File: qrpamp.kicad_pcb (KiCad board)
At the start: 2 copper layers, 106 parts, among them K1 BAND3_IN, K2 BAND2_IN, K3 BAND1_IN, K4 BAND3_OUT, K5 BAND2_OUT, K6 BAND1_OUT, K7 ANT_RLY, P1 PWR, P2 PWR_SW, P3 SWD, P4 ANT, P5 RADIO, P6 PTT_IN, P7 Thumb-Joystick, Q1 MMBT6427, Q2 MMBF170, Q3 IRF510, Q4 IRF510, SW1 SW_PUSH, T1 8:8, T2 8:8, T3 2:3, T4 12:1, T5 1:12, U1 LM7805, U2 LM3940, U3 LCD-2x16, U4 STM32F401xB/C-LQFP

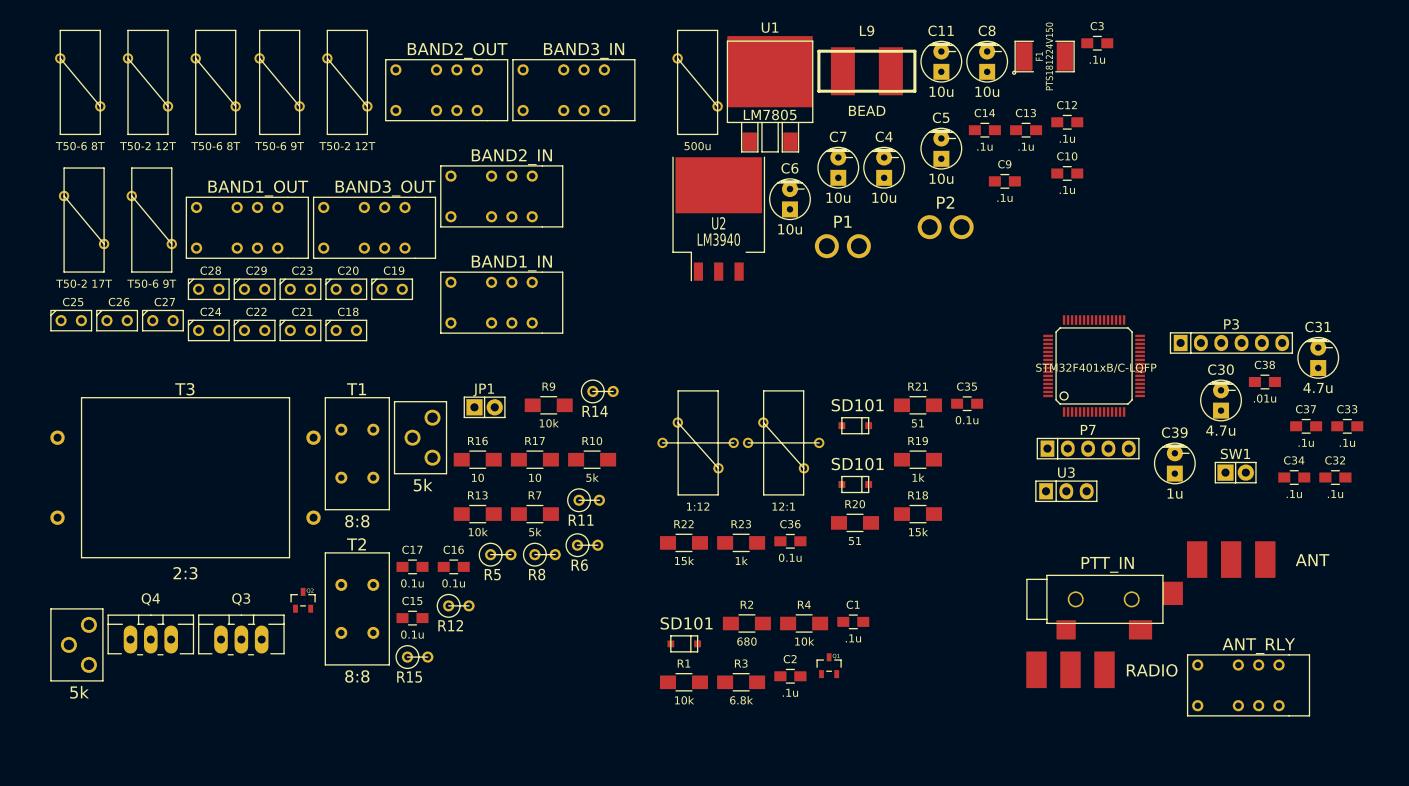
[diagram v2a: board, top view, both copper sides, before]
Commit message: All layed out
Several net errors fixed, and some mcu pins reassigned for better layout.
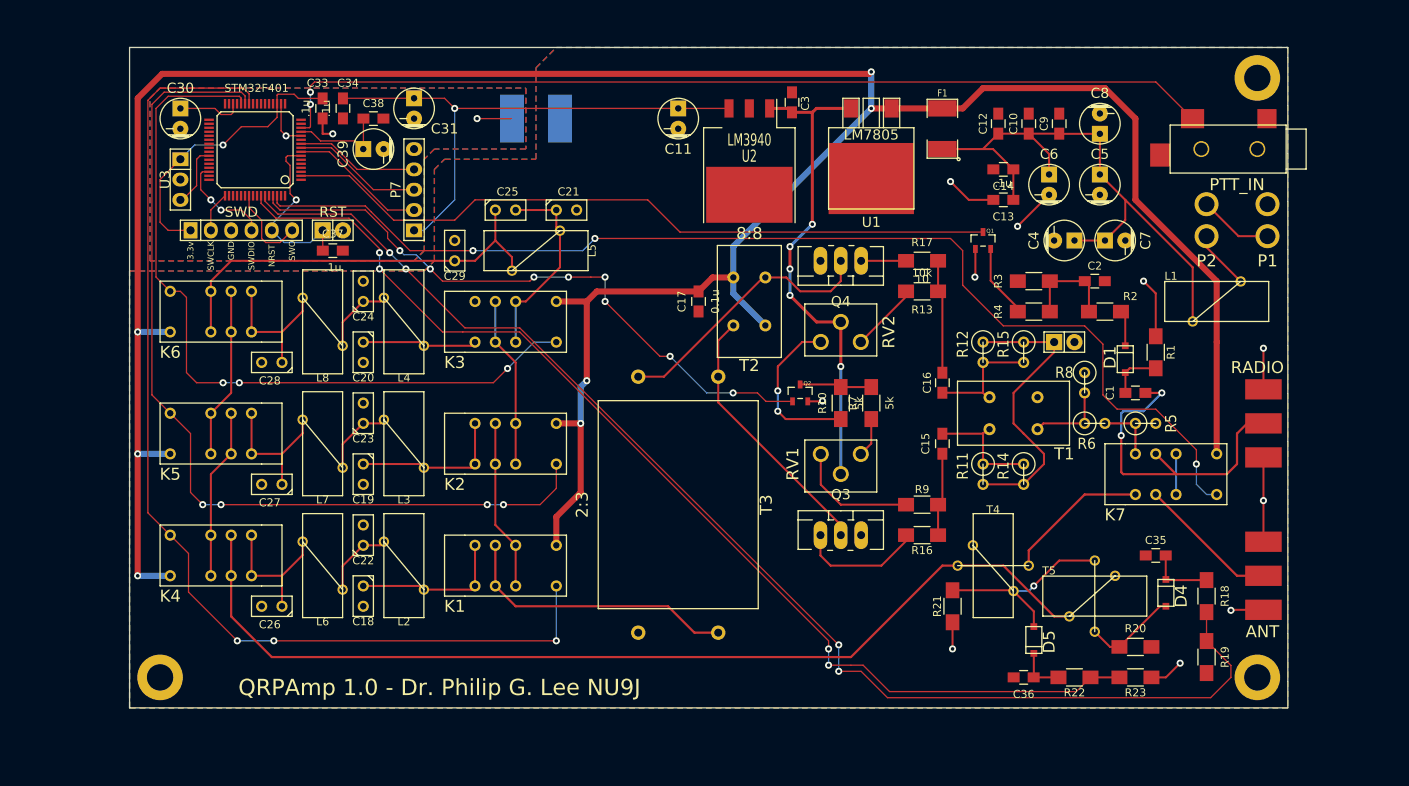
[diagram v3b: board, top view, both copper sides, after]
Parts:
- removed C32: .1u, Capacitors_SMD:C_0805_HandSoldering
- added Mounting Hole: VAL**, nu9j-footprints:MountingHole4-40, F.Cu at (86.4, 128.3)
- added Mounting Hole: VAL**, nu9j-footprints:MountingHole4-40, F.Cu at (223.5, 128.3)
- added Mounting Hole: VAL**, nu9j-footprints:MountingHole4-40, F.Cu at (223.5, 53.3)
- U4: value STM32F401xB/C-LQFP -> STM32F401
- moved C30 134.8 mm to (88.9, 58.4), turned to 180 degrees
- moved C33 134.1 mm to (106.7, 57.1), turned to 270 degrees
- moved C34 127.5 mm to (109.2, 57.1), turned to 270 degrees
- moved SWD 124.6 mm to (96.5, 72.4)
- moved C37 123.6 mm to (108.0, 74.9)
- moved U3 117.4 mm to (88.9, 66.0), turned to 270 degrees
- moved C31 117.2 mm to (118.1, 57.1), turned to 180 degrees
- moved RST 116.9 mm to (108.0, 72.4)
- moved C38 116.2 mm to (113.0, 58.4)
- moved C39 107.6 mm to (113.0, 62.2), turned to 270 degrees
- moved U4 99.7 mm to (104.0, 66.1), turned to 90 degrees
- moved Q4 98.4 mm to (171.4, 76.2), turned to 180 degrees
- moved RV1 97.9 mm to (171.4, 101.6), turned to 90 degrees
- moved P7 90.3 mm to (118.1, 67.3), turned to 90 degrees
- moved R15 84.8 mm to (194.3, 87.6), turned to 270 degrees
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- renumbered SW1 to RST, P3 to SWD
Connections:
- K1 pad 1: Net-(K1-Pad1) -> +12V
- K1 pad 10: (no net) -> Net-(K1-Pad10)
- K1 pad 12: /Amplifier/amp_out -> /Band Filters/bandfilter_3sel
- K1 pad 3: Net-(K1-Pad14) -> Net-(K1-Pad10)
- K1 pad 4: (no net) -> /Amplifier/amp_out
- K1 pad 5: /Amplifier/amp_out -> Net-(C18-Pad1)
- K1 pad 8: +12V -> Net-(C18-Pad1)
- K1 pad 9: /Band Filters/bandfilter_3sel -> /Amplifier/amp_out
- K2 pad 1: Net-(C19-Pad1) -> +12V
- K2 pad 10: (no net) -> Net-(K2-Pad10)
- K2 pad 12: Net-(K1-Pad14) -> /Band Filters/bandfilter_2sel
- K2 pad 3: Net-(K2-Pad14) -> Net-(K2-Pad10)
- K2 pad 4: (no net) -> Net-(K1-Pad10)
- K2 pad 5: Net-(K1-Pad14) -> Net-(C19-Pad1)
- K2 pad 8: +12V -> Net-(C19-Pad1)
- K2 pad 9: /Band Filters/bandfilter_2sel -> Net-(K1-Pad10)
- K3 pad 1: Net-(C20-Pad1) -> +12V
- K3 pad 10: (no net) -> Net-(C21-Pad1)
- K3 pad 12: Net-(K2-Pad14) -> /Band Filters/bandfilter_1sel
- K3 pad 4: (no net) -> Net-(K2-Pad10)
- K3 pad 5: Net-(K2-Pad14) -> Net-(C20-Pad1)
- K3 pad 8: +12V -> Net-(C20-Pad1)
- K3 pad 9: /Band Filters/bandfilter_1sel -> Net-(K2-Pad10)
- K4 pad 1: Net-(C26-Pad1) -> +12V
- K4 pad 10: (no net) -> Net-(K4-Pad10)
- K4 pad 12: /Band Filters/bandfilter_out -> /Band Filters/bandfilter_3sel
- K4 pad 3: Net-(K4-Pad14) -> Net-(K4-Pad10)
- K4 pad 4: (no net) -> /Band Filters/bandfilter_out
- K4 pad 5: /Band Filters/bandfilter_out -> Net-(C26-Pad1)
- K4 pad 8: +12V -> Net-(C26-Pad1)
- K4 pad 9: /Band Filters/bandfilter_3sel -> /Band Filters/bandfilter_out
- K5 pad 1: Net-(C27-Pad1) -> +12V
- K5 pad 10: (no net) -> Net-(K5-Pad10)
- K5 pad 12: Net-(K4-Pad14) -> /Band Filters/bandfilter_2sel
- K5 pad 3: Net-(K5-Pad14) -> Net-(K5-Pad10)
- K5 pad 4: (no net) -> Net-(K4-Pad10)
- K5 pad 5: Net-(K4-Pad14) -> Net-(C27-Pad1)
- K5 pad 8: +12V -> Net-(C27-Pad1)
- K5 pad 9: /Band Filters/bandfilter_2sel -> Net-(K4-Pad10)
- K6 pad 1: Net-(C28-Pad1) -> +12V
- K6 pad 10: (no net) -> Net-(C25-Pad1)
- K6 pad 12: Net-(K5-Pad14) -> /Band Filters/bandfilter_1sel
- K6 pad 4: (no net) -> Net-(K5-Pad10)
- K6 pad 5: Net-(K5-Pad14) -> Net-(C28-Pad1)
- K6 pad 8: +12V -> Net-(C28-Pad1)
- K6 pad 9: /Band Filters/bandfilter_1sel -> Net-(K5-Pad10)
- K7 pad 1: /Amplifier/amp_in -> +12V
- K7 pad 10: (no net) -> Net-(K7-Pad10)
- K7 pad 12: Net-(K7-Pad12) -> /RF In/Out/ant_sw_rly
- K7 pad 3: Net-(K7-Pad14) -> Net-(K7-Pad10)
- K7 pad 4: (no net) -> /RF In/Out/raw_input
- K7 pad 5: /RF In/Out/raw_input -> /Amplifier/amp_in
- K7 pad 8: +12V -> /RF In/Out/from_final
- K7 pad 9: /RF In/Out/ant_sw_rly -> Net-(K7-Pad9)
- L2 pad 1: Net-(K1-Pad1) -> Net-(C18-Pad1)
- P4 pad 1: Net-(K7-Pad12) -> Net-(K7-Pad9)
- Q4 pad S: Net-(Q4-PadS) -> GND
- R20 pad 1: Net-(R20-Pad1) -> Net-(D4-Pad1)
- R21 pad 1: Net-(R21-Pad1) -> Net-(D5-Pad1)
- U4 pad 14: Net-(U4-Pad14) -> /Microcontroller/mcu_ptt
- U4 pad 2: Net-(U4-Pad2) -> /Microcontroller/mcu_rfdet
- U4 pad 26: /Band Filters/bandfilter_1sel -> /Band Filters/bandfilter_3sel
- U4 pad 28: /Band Filters/bandfilter_3sel -> /Band Filters/bandfilter_1sel
- U4 pad 56: /Microcontroller/mcu_rfdet -> Net-(U4-Pad56)
- U4 pad 57: /Microcontroller/mcu_ptt -> Net-(U4-Pad57)
- U4 pad 58: /Microcontroller/mcu_swr_fwd -> /Microcontroller/mcu_swr_ref
- U4 pad 59: /Microcontroller/mcu_swr_ref -> /Microcontroller/mcu_swr_fwd
- U4 pad 61: /RF In/Out/ant_sw_rly -> /Amplifier/amp_on
- U4 pad 62: /Amplifier/amp_on -> /RF In/Out/ant_sw_rly
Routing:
- net +12V: track 0.00 -> 345.7 mm, vias 0 -> 7
- net /Microcontroller/mcu_swr_fwd: track 0.00 -> 159.5 mm, vias 0 -> 4
- net /RF In/Out/ant_sw_rly: track 0.00 -> 143.5 mm, vias 0 -> 3
- net /Microcontroller/mcu_swr_ref: track 0.00 -> 137.5 mm, vias 0 -> 4
- net /Band Filters/bandfilter_3sel: track 0.00 -> 133.8 mm, vias 0 -> 3
- net /Band Filters/bandfilter_out: track 0.00 -> 124.4 mm
- net /Microcontroller/mcu_ptt: track 0.00 -> 118.7 mm, vias 0 -> 2
- net +3.3V: track 0.00 -> 115.5 mm, vias 0 -> 2
- net /Band Filters/bandfilter_2sel: track 0.00 -> 114.2 mm, vias 0 -> 4
- net /Band Filters/bandfilter_1sel: track 0.00 -> 96.6 mm, vias 0 -> 3
- net /Microcontroller/mcu_rfdet: track 0.00 -> 90.3 mm
- net /Amplifier/amp_on: track 0.00 -> 78.8 mm, vias 0 -> 8
- net Net-(C10-Pad1): track 0.00 -> 73.5 mm
- net +5V: track 0.00 -> 61.3 mm, vias 0 -> 5
- net Net-(C25-Pad1): track 0.00 -> 52.5 mm
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- added copper zone on B.Cu, net DGND
- added copper zone on F.Cu, net DGND
- added copper zone on B.Cu, net GND
- added copper zone on F.Cu, net GND
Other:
- board outline added: 144.8 x 82.6 mm
- net class 1A added: clearance 0.254, trace_width 0.381, via_dia 0.889, via_drill 0.635
- net class 2A added: clearance 0.254, trace_width 0.762, via_dia 0.889, via_drill 0.635
- net class 50-ohm added: clearance 0.254, trace_width 0.2794, via_dia 0.889, via_drill 0.635
- net class digital-signal added: clearance 0.1524, trace_width 0.1524, via_dia 0.889, via_drill 0.635
- rule trace_min: 0.254 -> 0.1524
- board text added: "3.3v"
- board text added: "GND"
- board text added: "NRST"
- board text added: "QRPAmp 1.0 - Dr. Philip G. Lee NU9J"
- board text added: "SWCLK"
- board text added: "SWDIO"
- board text added: "SWO"

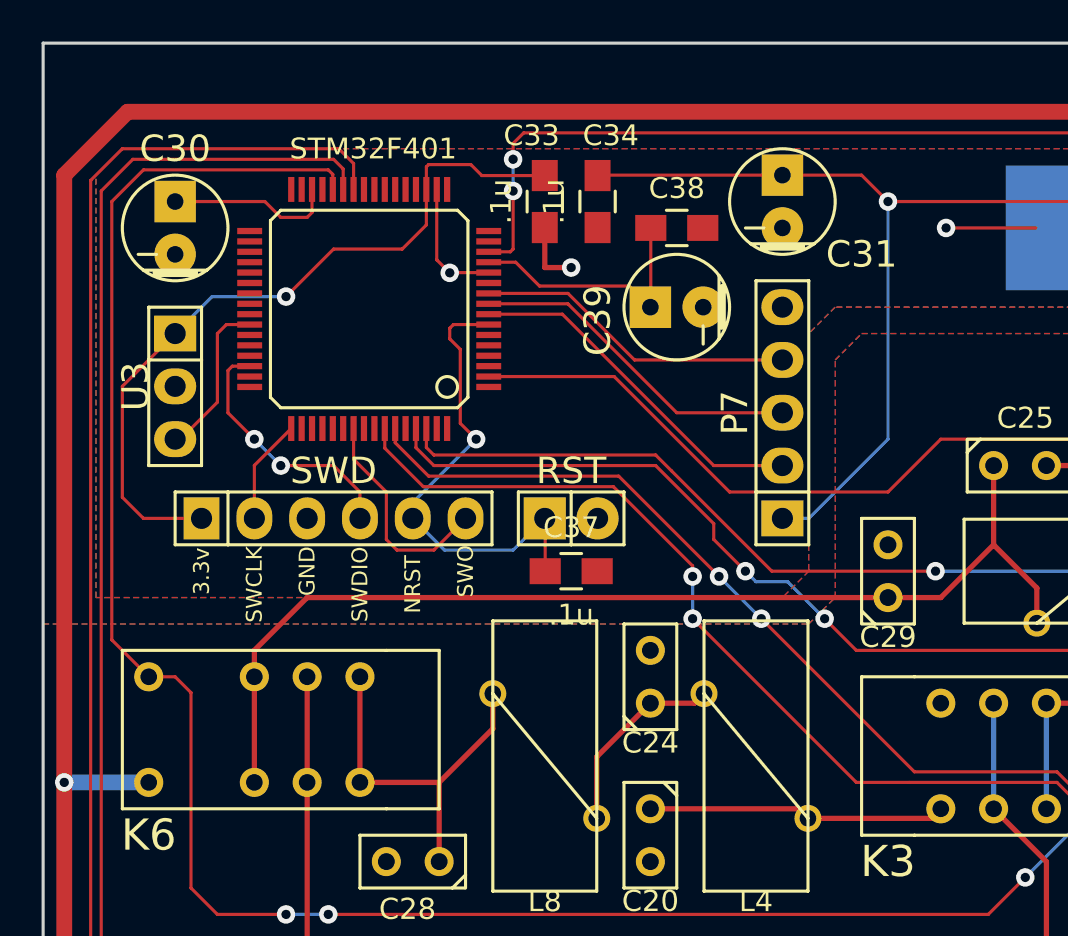
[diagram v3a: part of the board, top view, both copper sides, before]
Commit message: Connected all mcu VSS and VDD pins.
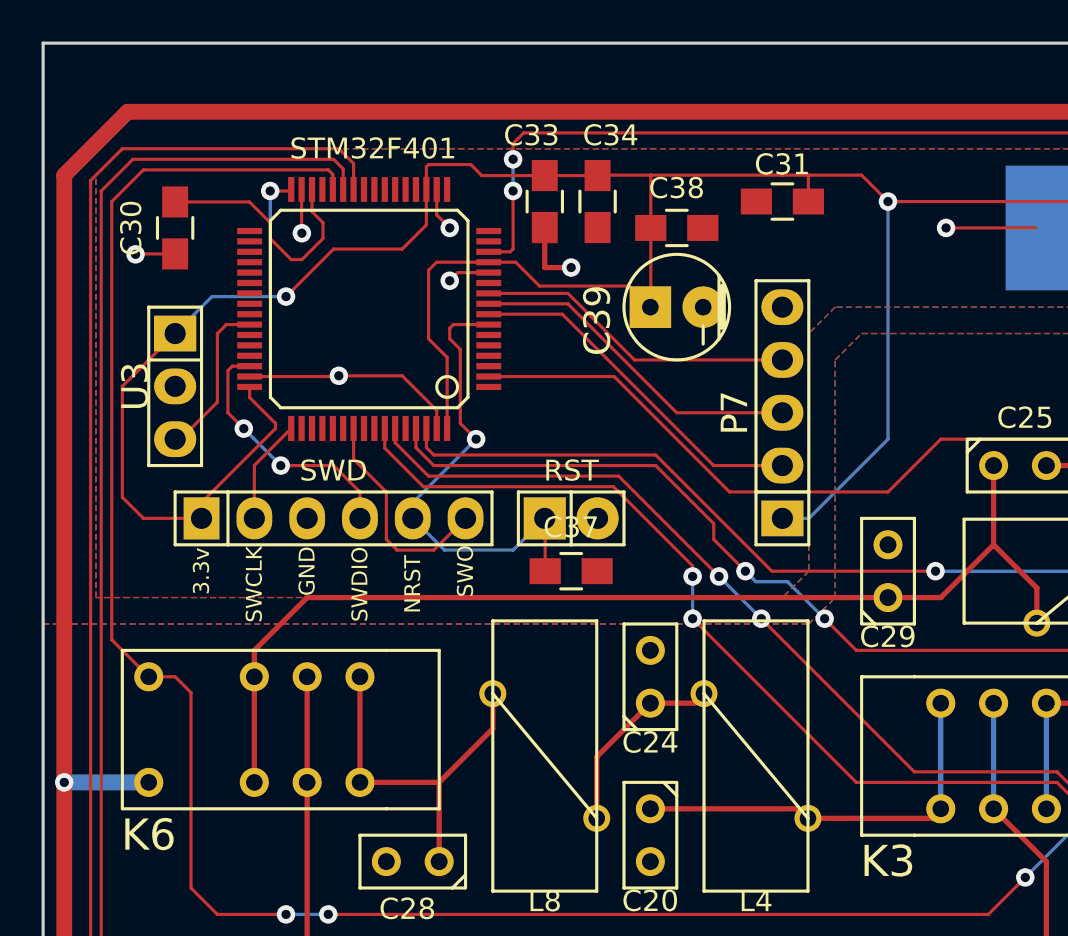
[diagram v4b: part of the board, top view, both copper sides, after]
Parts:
- C30, C31: footprint Capacitors_ThroughHole:Capacitor5x11RM2.5 -> Capacitors_SMD:C_0805_HandSoldering
- turned C30 to 90 degrees
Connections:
- C30 pad 1: Net-(C30-Pad1) -> DGND
- C30 pad 2: DGND -> Net-(C30-Pad2)
- U4 pad 30: Net-(C30-Pad1) -> Net-(C30-Pad2)
- U4 pad 31: Net-(U4-Pad31) -> DGND
- U4 pad 32: Net-(U4-Pad32) -> +3.3V
- U4 pad 47: Net-(U4-Pad47) -> DGND
- U4 pad 48: Net-(U4-Pad48) -> +3.3V
- U4 pad 63: Net-(U4-Pad63) -> DGND
- U4 pad 64: Net-(U4-Pad64) -> +3.3V
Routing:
- net +3.3V: track 115.5 -> 147.4 mm, vias 2 -> 3
- net DGND: track 9.34 -> 21.9 mm, vias 2 -> 6
- net Net-(C30-Pad2): track 0.00 -> 11.7 mm
- net Net-(C30-Pad1): track 8.11 -> 0.00 mm
- net Net-(C20-Pad1): track 14.4 -> 19.4 mm

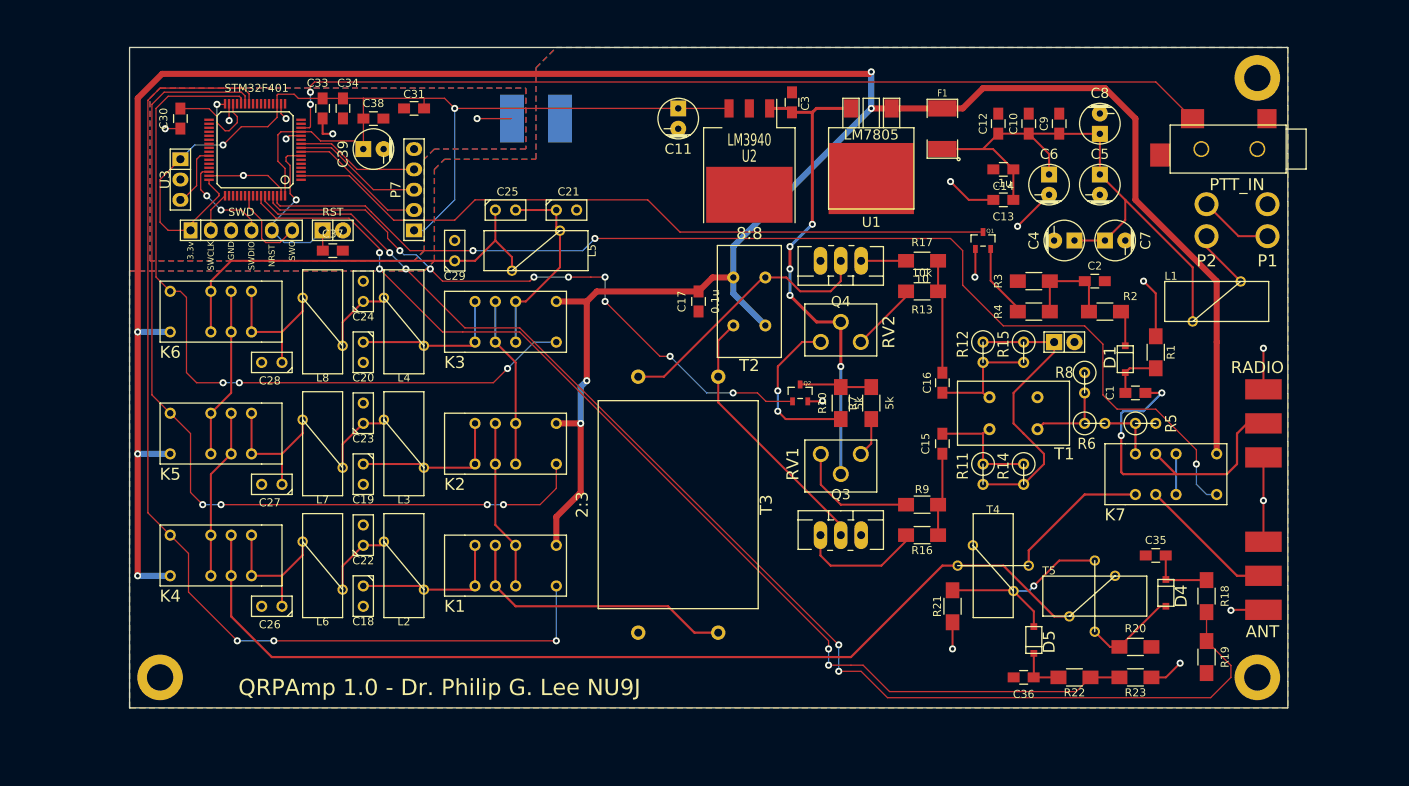
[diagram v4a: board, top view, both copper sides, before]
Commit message: Added ADC input resistors
Also reassigned the band switch pins on the 401 for better layout.
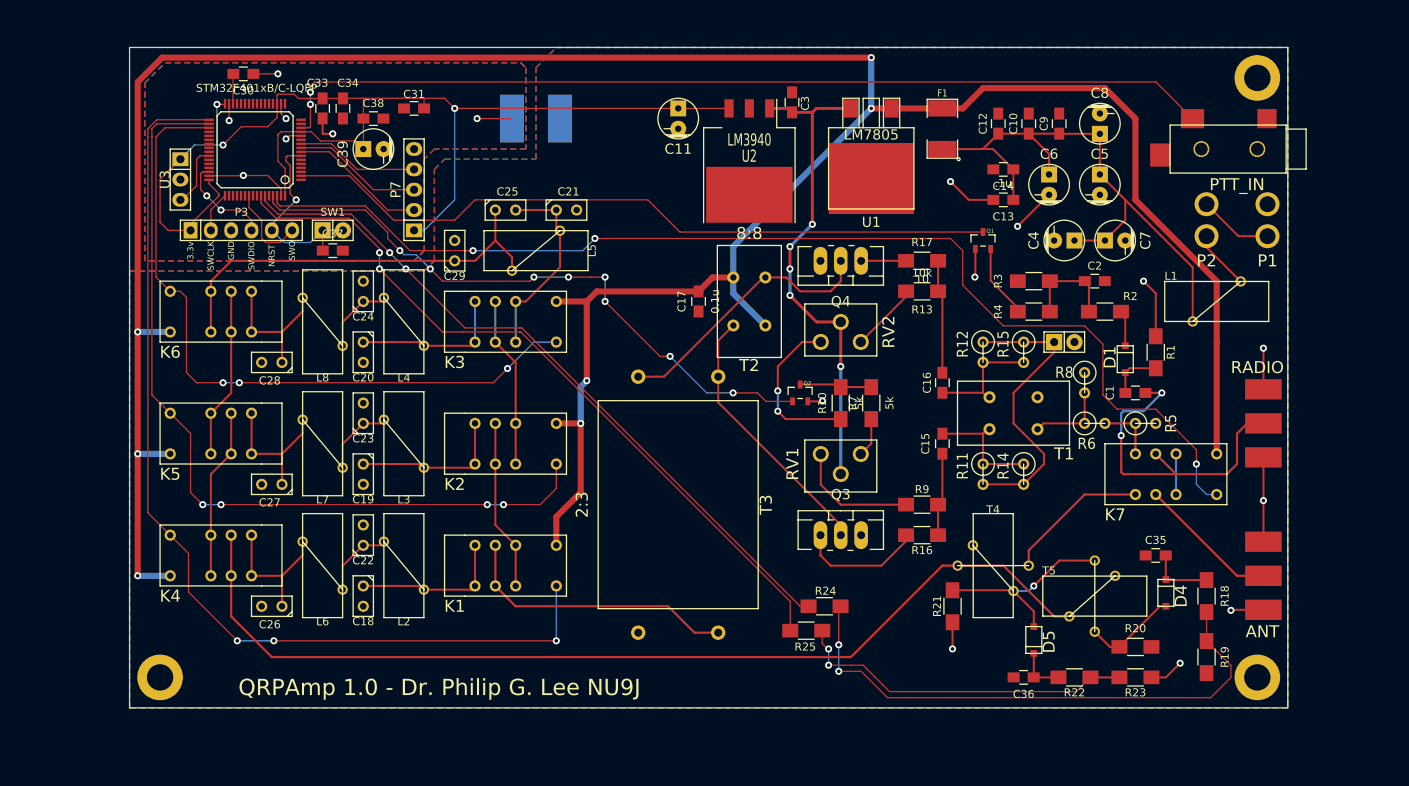
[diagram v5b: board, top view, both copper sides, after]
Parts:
- removed RST: SW_PUSH, Pin_Headers:Pin_Header_Straight_1x02
- removed SWD: SWD, Pin_Headers:Pin_Header_Straight_1x06
- added P3: SWD, Pin_Headers:Pin_Header_Straight_1x06, F.Cu at (96.5, 72.4)
- added R24: 50k, Resistors_SMD:R_1206_HandSoldering, F.Cu at (167.1, 122.4)
- added R25: 50k, Resistors_SMD:R_1206_HandSoldering, F.Cu at (169.4, 119.4)
- added SW1: SW_PUSH, Pin_Headers:Pin_Header_Straight_1x02, F.Cu at (108.0, 72.4)
- U4: value STM32F401 -> STM32F401xB/C-LQFP
- moved C30 9.66 mm to (96.8, 52.8), turned to 180 degrees
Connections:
- U4 pad 26: /Band Filters/bandfilter_3sel -> Net-(U4-Pad26)
- U4 pad 27: /Band Filters/bandfilter_2sel -> Net-(U4-Pad27)
- U4 pad 28: /Band Filters/bandfilter_1sel -> Net-(U4-Pad28)
- U4 pad 33: Net-(U4-Pad33) -> /Band Filters/bandfilter_3sel
- U4 pad 34: Net-(U4-Pad34) -> /Band Filters/bandfilter_2sel
- U4 pad 35: Net-(U4-Pad35) -> /Band Filters/bandfilter_1sel
- U4 pad 58: /Microcontroller/mcu_swr_ref -> Net-(R24-Pad1)
- U4 pad 59: /Microcontroller/mcu_swr_fwd -> Net-(R25-Pad2)
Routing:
- net /Microcontroller/mcu_swr_ref: track 137.5 -> 43.2 mm, vias 4 -> 2
- net Net-(R24-Pad1): track 0.00 -> 92.8 mm, vias 0 -> 2
- net /Microcontroller/mcu_swr_fwd: track 159.5 -> 69.1 mm, vias 4 -> 2
- net Net-(R25-Pad2): track 0.00 -> 89.6 mm, vias 0 -> 2
- net /Band Filters/bandfilter_3sel: track 133.8 -> 123.5 mm
- net /Band Filters/bandfilter_2sel: track 114.2 -> 105.1 mm
- net /Band Filters/bandfilter_1sel: track 96.6 -> 88.1 mm
- net Net-(C30-Pad2): track 11.7 -> 3.75 mm
- net +12V: track 345.7 -> 349.4 mm
- net DGND: track 21.9 -> 23.1 mm
